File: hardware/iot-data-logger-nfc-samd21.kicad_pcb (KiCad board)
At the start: 2 copper layers, 75 x 56 mm, 57 parts, among them IC1 ST25DV04KC, IC2 BU27030NUC-E2, J1 ARM-JTAG-SWD-10, J2 USB_C_Receptacle_USB2.0, Q1 IRLML6401, U1 LD1117S33TR, U2 ATSAMD21E17D-AUT, U3 AT25DF041B-XMHN-B, U4 ATECC608A, U5 TPD2E009DBZR, U6 SHT30-DIS, U7 ICM-42670-P, Y1 32.768K-38-SR, Y2 KX-3HT 8.0 MHz

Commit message: PCB: add qr to github repo
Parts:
- added G***: LOGO, LOGO, F.Cu at (109.5, 64.3)
- moved REF2 1.78 mm to (109.5, 93.0)

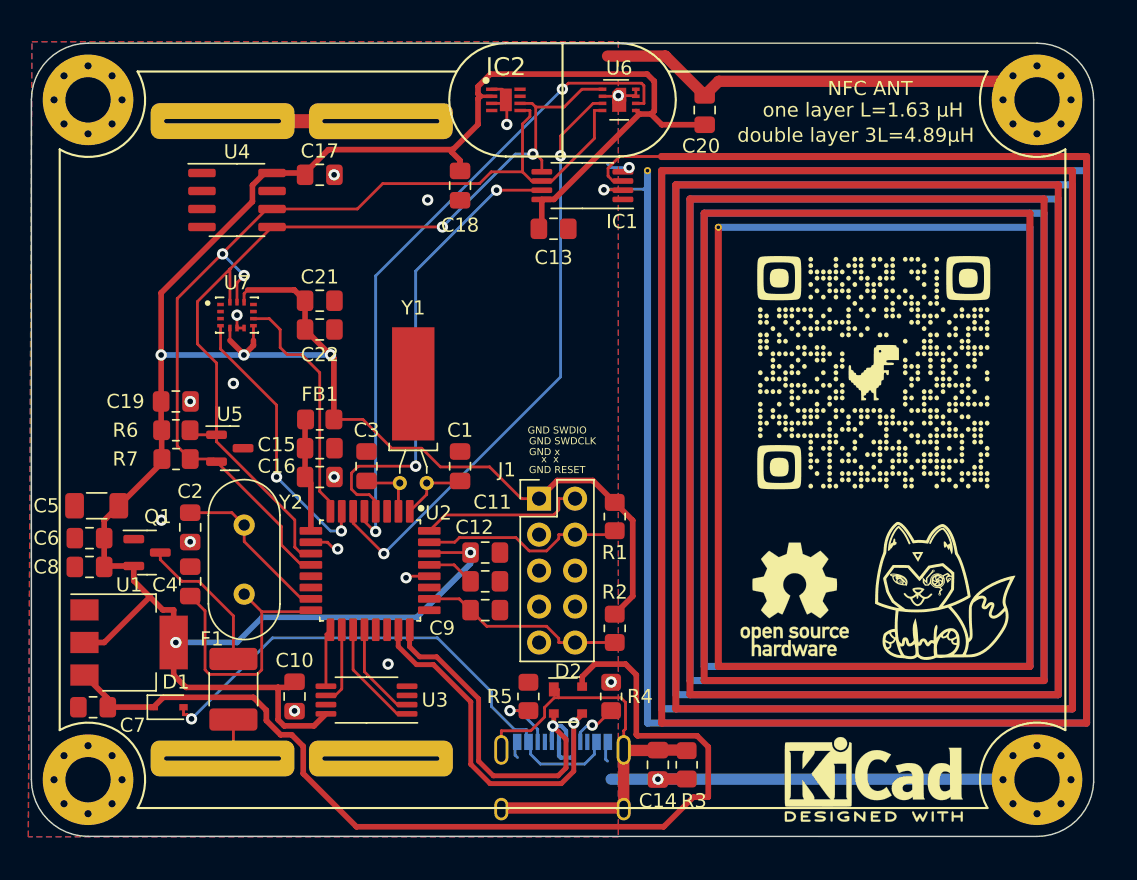
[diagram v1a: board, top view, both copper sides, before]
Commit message: add enclosure, bom docs
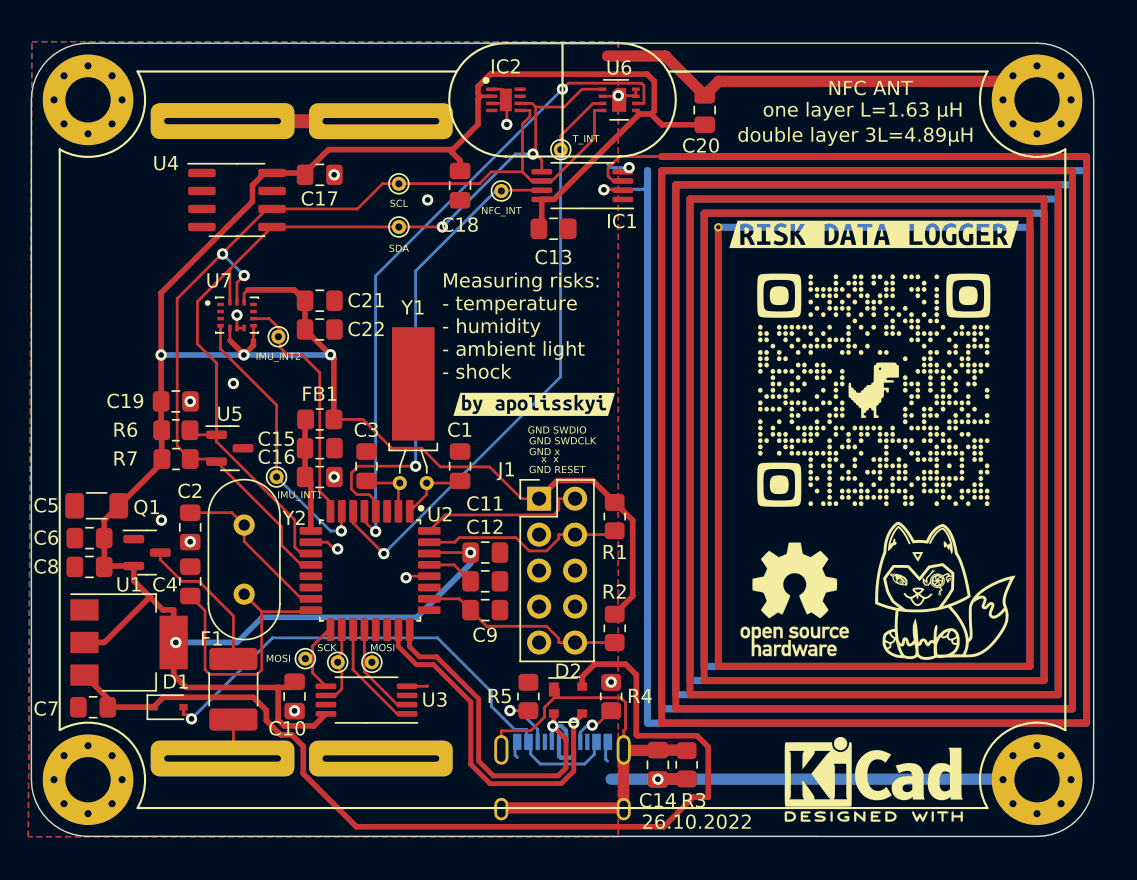
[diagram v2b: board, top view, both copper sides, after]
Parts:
- added TP1: TestPoint_Probe, TestPoint:TestPoint_THTPad_D1.0mm_Drill0.5mm, F.Cu at (75.9, 54.0)
- added TP2: TestPoint_Probe, TestPoint:TestPoint_THTPad_D1.0mm_Drill0.5mm, F.Cu at (75.9, 50.9)
- added TP3: TestPoint_Probe, TestPoint:TestPoint_THTPad_D1.0mm_Drill0.5mm, F.Cu at (69.3, 84.5)
- added TP4: TestPoint_Probe, TestPoint:TestPoint_THTPad_D1.0mm_Drill0.5mm, F.Cu at (71.6, 84.7)
- added TP5: TestPoint_Probe, TestPoint:TestPoint_THTPad_D1.0mm_Drill0.5mm, F.Cu at (83.2, 51.4)
- added TP6: TestPoint_Probe, TestPoint:TestPoint_THTPad_D1.0mm_Drill0.5mm, F.Cu at (74.0, 84.7)
- added TP7: TestPoint_Probe, TestPoint:TestPoint_THTPad_D1.0mm_Drill0.5mm, F.Cu at (87.4, 48.5)
- added TP8: TestPoint_Probe, TestPoint:TestPoint_THTPad_D1.0mm_Drill0.5mm, F.Cu at (67.3, 71.6)
- added TP9: TestPoint_Probe, TestPoint:TestPoint_THTPad_D1.0mm_Drill0.5mm, F.Cu at (67.4, 61.7)
- added kibuzzard-6359939A: G***, kibuzzard-6359939A, F.Cu at (85.5, 66.5)
- added kibuzzard-63599401: G***, kibuzzard-63599401, F.Cu at (109.5, 54.5)
- moved G*** 1.24 mm to (109.5, 65.5)
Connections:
- net RESET renamed ~RESET
- net TEMP_RESET renamed ~TEMP_RESET
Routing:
- net MOSI: track 4.12 -> 5.93 mm
- net GND: track 81.0 -> 82.5 mm, vias 17 -> 16
- net MISO: track 6.93 -> 7.52 mm
- net TEMP_INT: vias 2 -> 1
- net NFC_INT: vias 2 -> 1
- net IMU_INT1: vias 2 -> 1
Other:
- board text added: "26.10.2022"
- board text added: "IMU_INT1"
- board text added: "IMU_INT2"
- board text added: "MOSI"
- board text added: "Measuring risks: - temperature - humidity - ambient light - shock"
- board text added: "NFC_INT"
- board text added: "SCK"
- board text added: "SCL"
- board text added: "SDA"
- board text added: "T_INT"
- board text added: "https://github.com/polesskiy-dev/iot-data-logger-nfc-samd21"

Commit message: upgrade PCB with CS pin, NFC pull-up
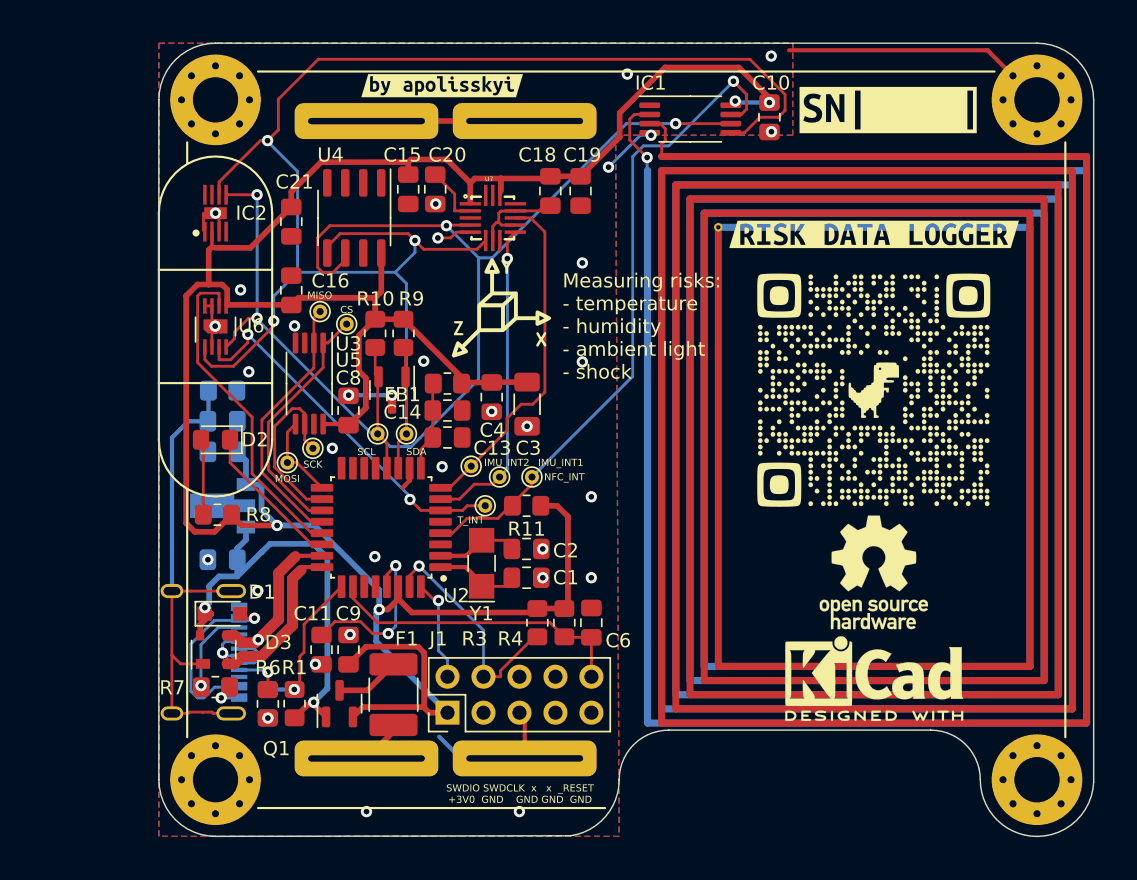
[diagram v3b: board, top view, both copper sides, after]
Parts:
- removed C17, C22: 100n, Capacitor_SMD:C_0805_2012Metric_Pad1.18x1.45mm_HandSolder
- removed G100: LOGO, LOGO
- removed the REF1 at (103.9, 80.3)
- removed the REF1 at (54.0, 45.0)
- removed the REF2 at (109.5, 93.0)
- removed the REF2 at (54.0, 93.0)
- removed Y2: KX-3HT 8.0 MHz, Crystal:Crystal_HC49-U_Vertical
- added D3: PRTR5V0U2X, Package_TO_SOT_SMD:SOT-143, F.Cu at (62.9, 83.8)
- added G***: LOGO, LOGO, F.Cu at (83.2, 59.7)
- added R10: 4k7, Resistor_SMD:R_0805_2012Metric_Pad1.20x1.40mm_HandSolder, F.Cu at (74.3, 61.5)
- added R11: 10k, Resistor_SMD:R_0805_2012Metric_Pad1.20x1.40mm_HandSolder, F.Cu at (85.0, 73.7)
- added R8: 1k, Resistor_SMD:R_0805_2012Metric_Pad1.20x1.40mm_HandSolder, F.Cu at (63.1, 74.3)
- added R9: 4k7, Resistor_SMD:R_0805_2012Metric_Pad1.20x1.40mm_HandSolder, F.Cu at (76.3, 61.5)
- added REF**: OSHW-Logo_7.5x8mm_SilkScreen, Symbol:OSHW-Logo_7.5x8mm_SilkScreen, F.Cu at (109.5, 78.4)
- added REF**: KiCad-Logo2_5mm_SilkScreen, Symbol:KiCad-Logo2_5mm_SilkScreen, F.Cu at (109.5, 85.9)
- added REF1: MountingHole_3.2mm_M3_Pad_Via, MountingHole:MountingHole_3.2mm_M3_Pad_Via, F.Cu at (63.0, 93.0)
- added REF2: MountingHole_3.2mm_M3_Pad_Via, MountingHole:MountingHole_3.2mm_M3_Pad_Via, F.Cu at (63.0, 45.0)
- added TP10: TestPoint_Probe, TestPoint:TestPoint_THTPad_D1.0mm_Drill0.5mm, F.Cu at (72.3, 60.8)
- added kibuzzard-638E88EA: G***, kibuzzard-638E88EA, F.Cu at (110.5, 45.7)
- C11: value 100n -> 1u
- C12: value 1u -> 4n7; moved to B.Cu
- C14: value 4n7 -> 10u
- C16, C8: value 10u -> 100n
- C18: value 100n -> 10u
- C2: value 16p -> 12p
- C3: value 12p -> 22u; footprint Capacitor_SMD:C_0805_2012Metric_Pad1.18x1.45mm_HandSolder -> Capacitor_SMD:C_1206_3216Metric_Pad1.33x1.80mm_HandSolder
- C4: value 16p -> 100n
- C5: value 22u -> 10u; footprint Capacitor_SMD:C_1206_3216Metric_Pad1.33x1.80mm_HandSolder -> Capacitor_SMD:C_0805_2012Metric_Pad1.18x1.45mm_HandSolder; moved to B.Cu
- C7, R2: moved to B.Cu
- D1: footprint Diode_SMD:D_SOD-323 -> Diode_SMD:D_SOD-323_HandSoldering
- D2: value PRTR5V0U2X -> LED; footprint Package_TO_SOT_SMD:SOT-143 -> LED_SMD:LED_0805_2012Metric_Pad1.15x1.40mm_HandSolder
- R1: value 1k -> 10k
- R3: value 1M -> 1k
- R4: value 5k1 -> 10k
- R5: value 5k1 -> 1M; moved to B.Cu
- R6, R7: value 4k7 -> 5k1
- U1: value LD1117S33TR -> L78L33_SOT89; footprint Package_TO_SOT_SMD:SOT-223-3_TabPin2 -> Package_TO_SOT_SMD:SOT-89-3; moved to B.Cu
- U7: value ICM-42670-P -> MMA8452Q; footprint footprints:IC_ICM-42670-P -> footprints:QFN-16_0.5MM-EXTRA
- Y1: value 32.768K-38-SR -> KX-327NHT; footprint Crystal:Crystal_C38-LF_D3.0mm_L8.0mm_Horizontal_1EP_style1 -> Crystal:Crystal_SMD_EuroQuartz_EQ161-2Pin_3.2x1.5mm_HandSoldering
- moved C10 52.9 mm to (102.1, 46.2)
- moved REF3 48.0 mm to (121.0, 45.0)
- moved REF4 48.0 mm to (121.0, 93.0)
- moved C6 35.9 mm to (89.5, 81.9), turned to 90 degrees
- moved U6 32.7 mm to (63.0, 61.0), turned to 90 degrees
- moved C19 32.2 mm to (88.8, 51.4), turned to -90 degrees
- moved D2 30.9 mm to (63.0, 69.0), turned to 180 degrees
- moved R5 30.5 mm to (63.5, 65.5), turned to 0 degrees
- moved C14 29.1 mm to (79.4, 66.9), turned to 0 degrees
- moved J2 28.3 mm to (61.0, 84.0), turned to 90 degrees
- moved R1 26.2 mm to (68.6, 87.6), turned to 90 degrees
- moved TP7 25.7 mm to (82.0, 73.7)
- moved R2 25.1 mm to (66.7, 87.6)
- moved C4 24.9 mm to (82.5, 66.0), turned to -90 degrees
- moved C2 23.8 mm to (85.0, 76.7), turned to 0 degrees
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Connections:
- C11 pad 1: +3V0 -> Net-(C11-Pad1)
- C13 pad 1: +3V0 -> Net-(C13-Pad1)
- C14 pad 1: Net-(C14-Pad1) -> Net-(C13-Pad1)
- C15 pad 1: Net-(C15-Pad1) -> +3V0
- C16 pad 1: Net-(C15-Pad1) -> +3V0
- C2 pad 1: XIN -> XOUT32
- C20 pad 1: +3V0 -> Net-(C20-Pad1)
- C3 pad 1: XOUT32 -> +3V0
- C4 pad 1: XOUT -> +3V0
- C5 pad 1: +3V0 -> +5V
- C6 pad 1: +3V0 -> ~RESET
- C7 pad 1: +5V -> +3V0
- C9 pad 1: ~RESET -> +3V0
- D2 pad 1: Net-(C14-Pad1) -> LED
- D2 pad 2: USB_D+ -> Net-(D2-Pad2)
- FB1 pad 2: Net-(C15-Pad1) -> Net-(C13-Pad1)
- J2 pad S1: Net-(C14-Pad1) -> Net-(C12-Pad1)
- Q1 pad 1: GND -> +5V
- R1 pad 1: +3V0 -> +5V
- R1 pad 2: SWDCLK -> USB_VBUS_SENSE
- R2 pad 1: +3V0 -> USB_VBUS_SENSE
- R2 pad 2: ~RESET -> GND
- R3 pad 1: Net-(C14-Pad1) -> +3V0
- R3 pad 2: GND -> SWDCLK
- R4 pad 1: GND -> +3V0
- R4 pad 2: Net-(J2-PadA5) -> ~RESET
- R5 pad 1: GND -> Net-(C12-Pad1)
- R5 pad 2: Net-(J2-PadB5) -> GND
- R6 pad 1: +3V0 -> GND
- R6 pad 2: SDA -> Net-(J2-PadA5)
- R7 pad 1: +3V0 -> GND
- R7 pad 2: SCL -> Net-(J2-PadB5)
- REF4 pad 1: GND -> (no net)
- TP5 pad 1: NFC_INT -> MISO
- TP6 pad 1: MISO -> NFC_INT
- U1 pad 1: GND -> +3V0
- U1 pad 2: +3V0 -> GND
- U2 pad 15: XIN -> unconnected-(U2-Pad15)
- U2 pad 16: XOUT -> unconnected-(U2-Pad16)
- U2 pad 21: unconnected-(U2-Pad21) -> _TEMP_RESET
- U2 pad 22: unconnected-(U2-Pad22) -> LED
- U2 pad 25: unconnected-(U2-Pad25) -> USB_VBUS_SENSE
- U2 pad 29: Net-(C12-Pad1) -> Net-(C11-Pad1)
- U2 pad 5: ~TEMP_RESET -> unconnected-(U2-Pad5)
- U2 pad 9: Net-(C15-Pad1) -> Net-(C13-Pad1)
- U6 pad 6: ~TEMP_RESET -> _TEMP_RESET
- U7 pad 1: unconnected-(U7-Pad1) -> +3V0
- U7 pad 10: unconnected-(U7-Pad10) -> GND
- U7 pad 11: unconnected-(U7-Pad11) -> IMU_INT2
- U7 pad 12: +3V0 -> GND
- U7 pad 13: SCL -> (no net)
- U7 pad 14: SDA -> +3V0
- U7 pad 2: unconnected-(U7-Pad2) -> Net-(C20-Pad1)
- U7 pad 3: unconnected-(U7-Pad3) -> (no net)
- U7 pad 4: IMU_INT1 -> SCL
- U7 pad 5: +3V0 -> GND
- U7 pad 6: GND -> SDA
- U7 pad 8: +3V0 -> (no net)
- U7 pad 9: IMU_INT2 -> IMU_INT1
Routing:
- net SDA: track 67.2 -> 117.4 mm, vias 2 -> 3
- net ~TEMP_RESET: track 46.3 -> 0.00 mm, vias 2 -> 0
- net +5V: track 70.3 -> 32.1 mm, vias 0 -> 2
- net Net-(C14-Pad1): track 33.3 -> 0.00 mm
- net Net-(C12-Pad1): track 3.39 -> 35.5 mm
- net GND: track 82.5 -> 55.0 mm, vias 16 -> 34
- net Net-(D1-Pad2): track 39.1 -> 13.9 mm
- net SCL: track 70.8 -> 94.3 mm, vias 2 -> 4
- net _TEMP_RESET: track 0.00 -> 23.3 mm
- net XOUT: track 19.3 -> 0.00 mm
- net +3V0: track 209.7 -> 193.2 mm, vias 5 -> 4
- net TEMP_INT: track 42.5 -> 26.2 mm, vias 1 -> 2
- net USB_D-: track 29.4 -> 15.3 mm
- net NFC_INT: track 33.7 -> 47.3 mm
- net Net-(C11-Pad1): track 0.00 -> 12.2 mm, vias 0 -> 2
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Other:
- board size 75 x 56 mm -> 66 x 56 mm
- board text added: "CS"
- board text added: "MISO"
- board text added: "SWDIO SWDCLK x x _RESET +3V0 GND GND GND GND"
- board text removed: "26.10.2022"
- board text removed: "GND RESET"
- board text removed: "GND SWDCLK"
- board text removed: "GND SWDIO"
- board text removed: "GND x"
- board text removed: "x x"

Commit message: shematics, PCB, BOM: update, prepare for SMT order, change light sensor to OPT3001
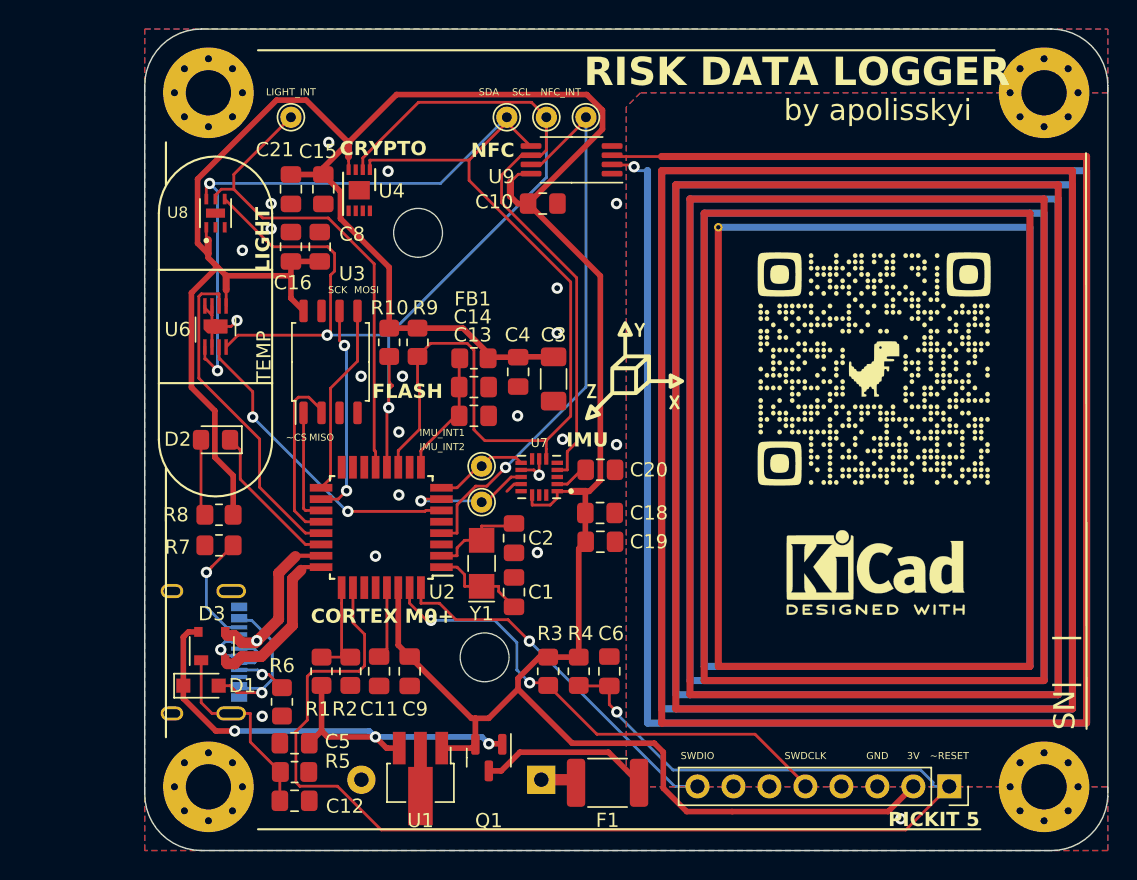
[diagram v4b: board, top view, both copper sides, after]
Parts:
- removed BT2: LR03 AAA 1Ah, footprints:BAT-AAA-LR03
- removed C7: 10u, Capacitor_SMD:C_0805_2012Metric_Pad1.18x1.45mm_HandSolder
- removed IC1: ST25DV04KC, Package_SO:TSSOP-8_4.4x3mm_P0.65mm
- removed IC2: BU27030NUC-E2, footprints:SON50P210X200X60-9N
- removed R11: 10k, Resistor_SMD:R_0805_2012Metric_Pad1.20x1.40mm_HandSolder
- removed the REF** at (109.5, 78.4)
- removed REF1, REF2, REF3, REF4: MountingHole_3.2mm_M3_Pad_Via, MountingHole:MountingHole_3.2mm_M3_Pad_Via
- removed TP10, TP3, TP4, TP5, TP7: TestPoint_Probe, TestPoint:TestPoint_THTPad_D1.0mm_Drill0.5mm
- removed U5: TPD2E009DBZR, Package_TO_SOT_SMD:SOT-23
- removed kibuzzard-6359939A: G***, kibuzzard-6359939A
- removed kibuzzard-63599401: G***, kibuzzard-63599401
- removed kibuzzard-638E88EA: G***, kibuzzard-638E88EA
- added H1: MountingHole_Pad, MountingHole:MountingHole_3.2mm_M3_Pad_Via, F.Cu at (62.5, 44.5)
- added H2: MountingHole_Pad, MountingHole:MountingHole_3.2mm_M3_Pad_Via, F.Cu at (121.5, 44.5)
- added H3: MountingHole_Pad, MountingHole:MountingHole_3.2mm_M3_Pad_Via, F.Cu at (121.5, 93.5)
- added H4: MountingHole_Pad, MountingHole:MountingHole_3.2mm_M3_Pad_Via, F.Cu at (62.5, 93.5)
- added NT1: NetTie_2, NetTie:NetTie-2_SMD_Pad0.5mm, F.Cu at (72.4, 48.5)
- added NT2: NetTie_2, NetTie:NetTie-2_SMD_Pad0.5mm, F.Cu at (88.6, 72.6)
- added NT3: NetTie_2, NetTie:NetTie-2_SMD_Pad0.5mm, F.Cu at (83.8, 51.3)
- added NT4: NetTie_2, NetTie:NetTie-2_SMD_Pad0.5mm, F.Cu at (62.5, 55.4)
- added NT5: NetTie_2, NetTie:NetTie-2_SMD_Pad0.5mm, F.Cu at (63.8, 57.9)
- added TP11: TestPoint_Probe, TestPoint:TestPoint_THTPad_D1.5mm_Drill0.7mm, F.Cu at (68.3, 46.2)
- added U8: OPT3001DNPR, Personal:SON65P200X200X65-7N, F.Cu at (63.0, 53.0)
- added U9: ST25DV04K, Package_SO:TSSOP-8_4.4x3mm_P0.65mm, F.Cu at (88.1, 49.2)
- BT1: value LR03 AAA 1Ah -> 2xAAA; footprint footprints:BAT-AAA-LR03 -> Battery:BatteryHolder_Keystone_2468_2xAAA
- C12, C5, R2, R5: moved to F.Cu
- F1: footprint Capacitor_SMD:C_1812_4532Metric_Pad1.57x3.40mm_HandSolder -> Fuse:Fuse_1812_4532Metric_Pad1.30x3.40mm_HandSolder
- J1: value ARM-JTAG-SWD-10 -> Pickit 5 Conn; footprint Connector_PinHeader_2.54mm:PinHeader_2x05_P2.54mm_Vertical -> Connector_PinSocket_2.54mm:PinSocket_1x08_P2.54mm_Vertical
- J2: value USB_C_Receptacle_USB2.0 -> USB Type-C
- TP1, TP2, TP6, TP8, TP9: footprint TestPoint:TestPoint_THTPad_D1.0mm_Drill0.5mm -> TestPoint:TestPoint_THTPad_D1.5mm_Drill0.7mm
- U1: value L78L33_SOT89 -> L78L33ABUTR; footprint Package_TO_SOT_SMD:SOT-89-3 -> Package_TO_SOT_SMD:SOT-89-3_Handsoldering; moved to F.Cu
- U2: value ATSAMD21E17D-AUT -> ATSAMD21E18A-AU; footprint footprints:QFP80P900X900X120-32N -> Package_QFP:TQFP-32_7x7mm_P0.8mm
- U3: value AT25DF041B-XMHN-B -> AT25DF321; footprint Package_SO:TSSOP-8_4.4x3mm_P0.65mm -> Package_SO:SOP-8_5.28x5.23mm_P1.27mm
- U4: value ATECC608A -> ATECC608A-MAHDA-S; footprint Package_SO:SOIC-8_3.9x4.9mm_P1.27mm -> Package_DFN_QFN:DFN-8-1EP_3x2mm_P0.5mm_EP1.3x1.5mm
- U7: value MMA8452Q -> MMA8452QR1; footprint footprints:QFN-16_0.5MM-EXTRA -> Personal:XDCR_MMA8452QR1
- Y1: value KX-327NHT -> SC-32S32.768
- moved BT1 45.0 mm to (86.0, 93.0), turned to 90 degrees
- moved J1 35.8 mm to (114.8, 93.5), turned to -90 degrees
- moved R5 27.4 mm to (68.6, 92.5)
- moved C12 27.3 mm to (68.6, 94.5)
- moved TP6 25.7 mm to (89.2, 46.2)
- moved TP2 25.3 mm to (86.4, 46.2)
- moved C19 24.8 mm to (90.2, 76.2), turned to 0 degrees
- moved U1 24.0 mm to (77.5, 93.2), turned to -90 degrees
- moved TP1 23.5 mm to (83.6, 46.2)
- moved C18 23.0 mm to (90.1, 74.2), turned to 0 degrees
- moved C20 23.0 mm to (90.2, 71.1), turned to 0 degrees
- moved U7 18.6 mm to (85.9, 71.6), turned to 180 degrees
- moved C10 17.1 mm to (86.1, 52.3), turned to 0 degrees
- moved F1 16.3 mm to (90.7, 93.2), turned to 180 degrees
- moved C5 13.9 mm to (68.6, 90.4)
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- renumbered G*** to G04
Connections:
- net FLASH_CS renamed ~FLASH_CS
- net _TEMP_RESET renamed ~TEMP_RESET
- BT1 pad 1: Net-(BT1-Pad1) -> Net-(BT1-+)
- F1 pad 2: Net-(BT2-Pad1) -> Net-(BT1-+)
- J1 pad 1: +3V0 -> ~RESET
- J1 pad 2: SWDIO -> +3V0
- J1 pad 4: SWDCLK -> unconnected-(J1-Pin_4-Pad4)
- J1 pad 5: GND -> SWDCLK
- J1 pad 8: unconnected-(J1-Pad8) -> SWDIO
- U2 pad 13: unconnected-(U2-Pad13) -> LIGHT_INT
- U2 pad 7: IMU_INT1 -> IMU_INT2
- U2 pad 8: IMU_INT2 -> IMU_INT1
- U4 pad 8: +3V0 -> Net-(U4-VCC)
- U6 pad 5: +3V0 -> Net-(U6-VDD)
- U7 pad 1: +3V0 -> Net-(U7-VDD)
- U7 pad 14: +3V0 -> Net-(U7-VDD)
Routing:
- net ~RESET: track 21.6 -> 97.0 mm, vias 0 -> 1
- net GND: track 55.0 -> 9.45 mm, vias 34 -> 21
- net LIGHT_INT: track 0.00 -> 35.0 mm
- net Net-(D3-GND): track 35.5 -> 13.8 mm
- net SWDCLK: track 16.7 -> 35.6 mm, vias 1 -> 2
- net SWDIO: track 7.29 -> 26.0 mm
- net IMU_INT1: track 22.6 -> 6.67 mm, vias 1 -> 0
- net IMU_INT2: track 24.7 -> 9.36 mm, vias 0 -> 1
- net SDA: track 117.4 -> 102.8 mm, vias 3 -> 2
- net +3V0: track 193.2 -> 206.7 mm, vias 4 -> 0
- net SCL: track 94.3 -> 106.4 mm, vias 4 -> 2
- net Net-(BT1-Pad1): track 11.2 -> 0.00 mm
- net ~FLASH_CS: track 17.8 -> 8.05 mm
- net +5V: track 32.1 -> 39.8 mm, vias 2 -> 3
- net Net-(Q1-D): track 4.57 -> 12.0 mm
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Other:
- board size 66 x 56 mm -> 68 x 58 mm
- board text added: "2xAAA 2.4-3.0V"
- board text added: "3V"
- board text added: "CORTEX M0+"
- board text added: "CRYPTO"
- board text added: "FLASH"
- board text added: "GND"
- board text added: "IMU"
- board text added: "LIGHT"
- board text added: "LIGHT_INT"
- board text added: "NFC"
- board text added: "PICKIT 5"
- board text added: "RISK DATA LOGGER"
- board text added: "SN| |"
- board text added: "SWDCLK"
- board text added: "SWDIO"
- board text added: "TEMP"
- board text added: "USB-C"
- board text added: "by apolisskyi"
- board text added: "~CS"
- board text added: "~RESET"
- board text removed: "CS"
- board text removed: "Measuring risks: - temperature - humidity - ambient light - shock"
- board text removed: "SWDIO SWDCLK x x _RESET +3V0 GND GND GND GND"
- board text removed: "T_INT"
- board text removed: "https://github.com/polesskiy-dev/iot-data-logger-nfc-samd21"
